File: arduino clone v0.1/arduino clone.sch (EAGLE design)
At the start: 21 parts, among them J202 FTDI Breakout Header, U101 ATMEGA328P_TQFP, U201 CH340G

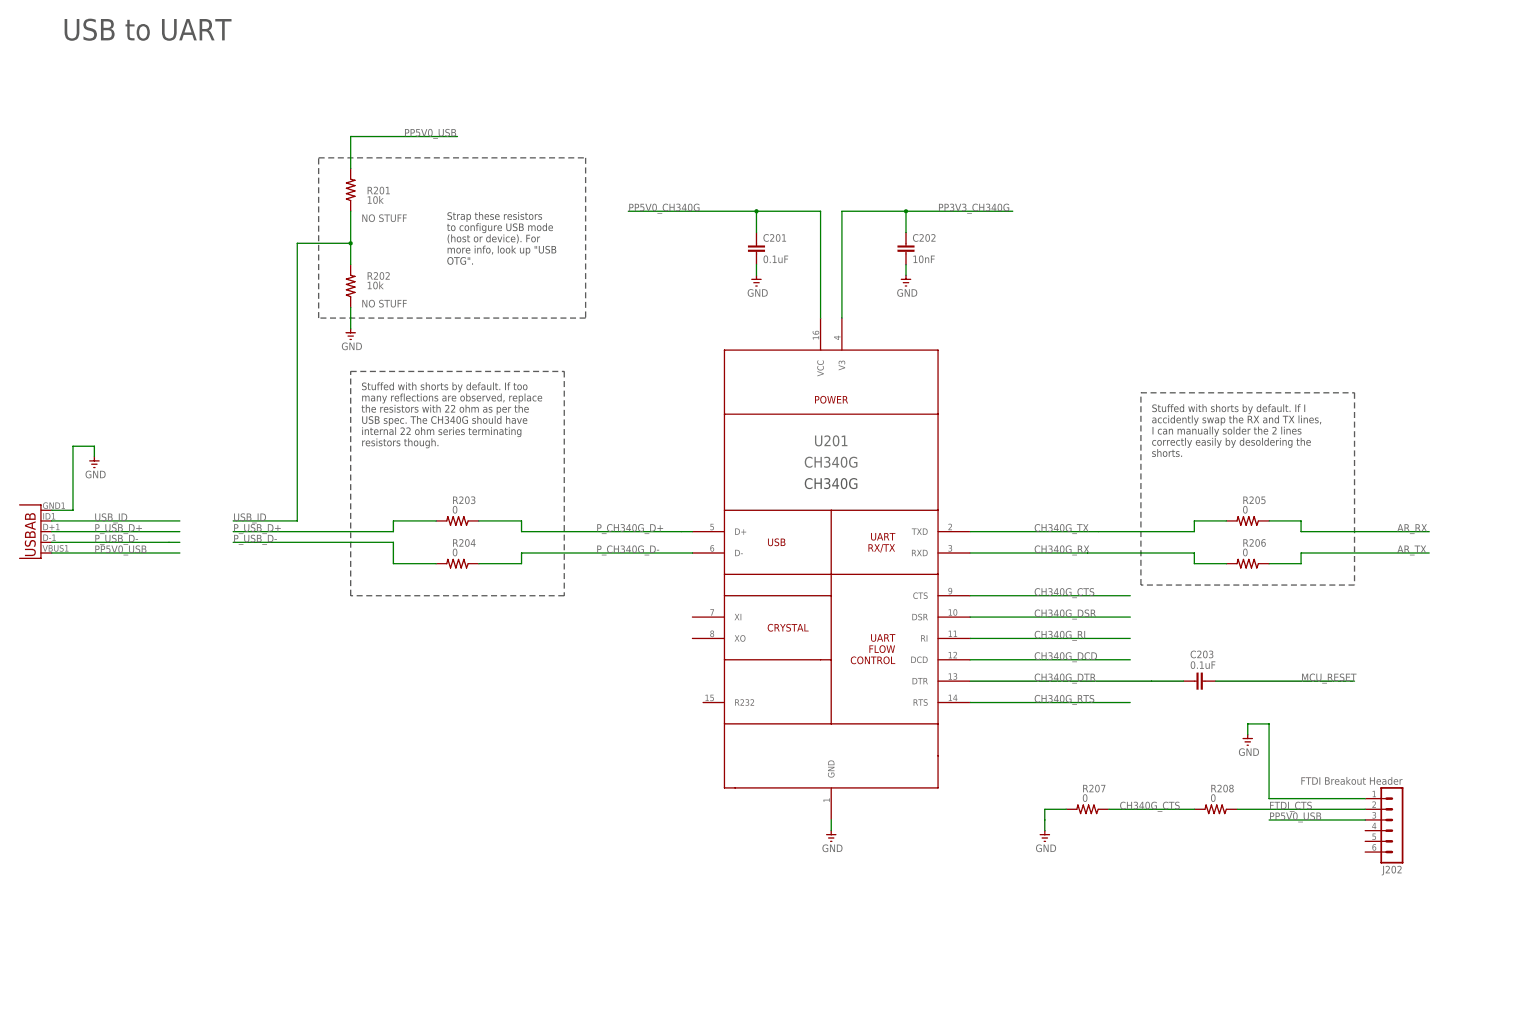
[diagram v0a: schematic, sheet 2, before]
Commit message: add FTDI RX and TX lines
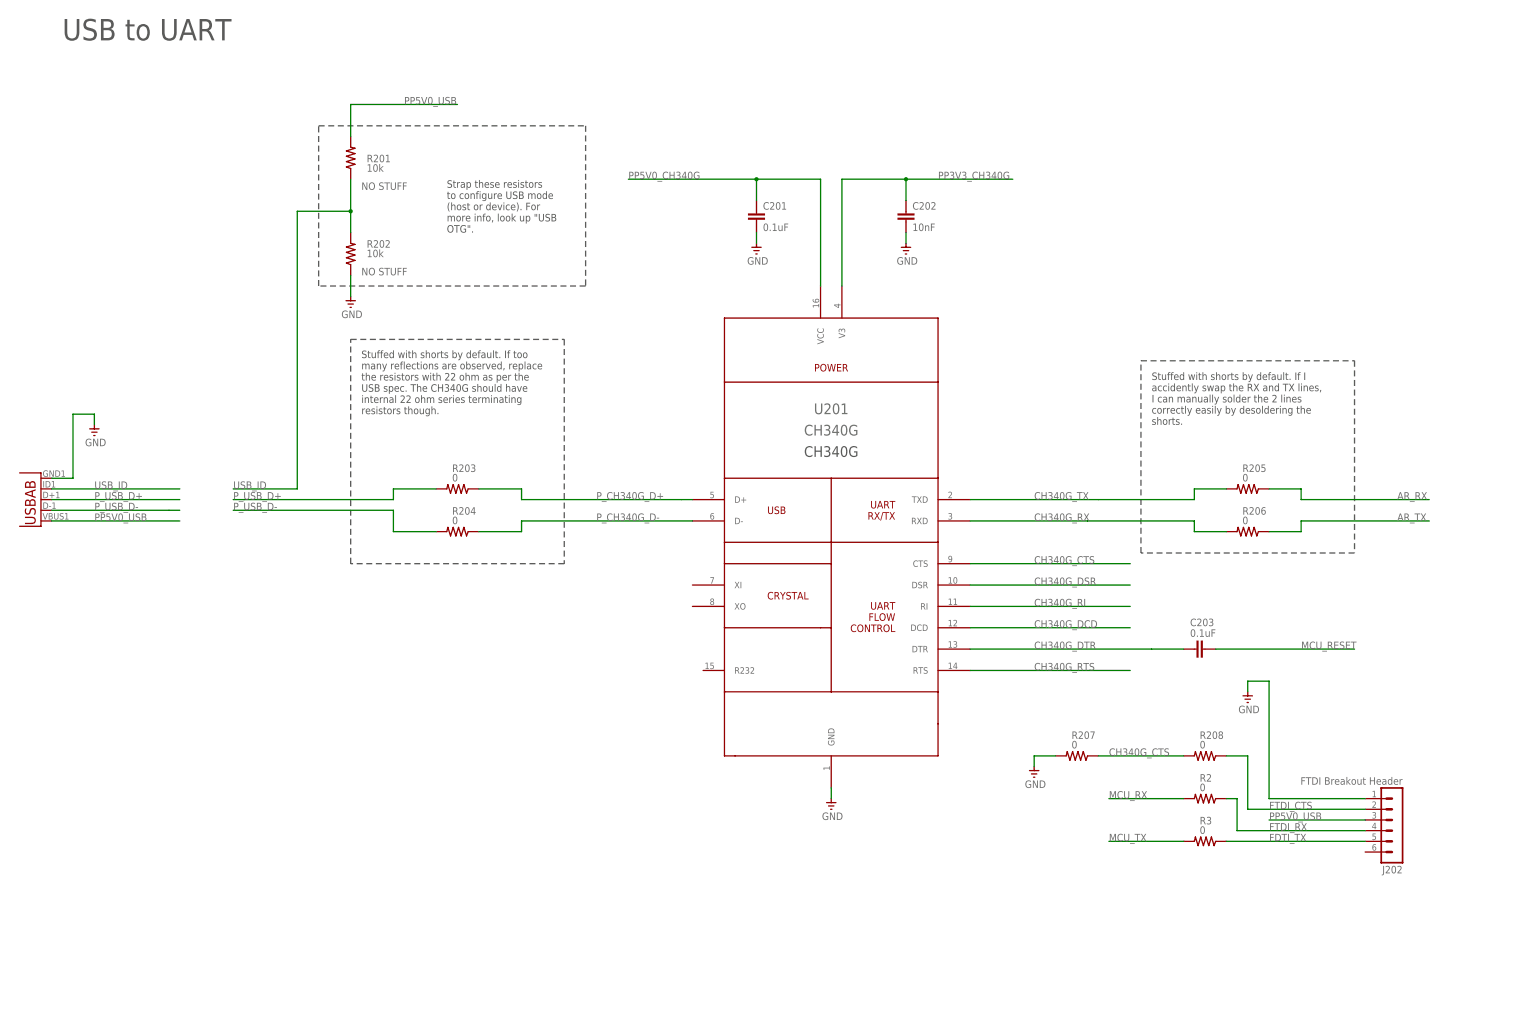
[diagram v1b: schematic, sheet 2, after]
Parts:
- added R2, R3: 0, adafruit:R-US_R0805
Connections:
- new net FDTI_TX: J202.5, R3.1
- new net FTDI_RX: J202.4, R2.1
- new net MCU_RX: R2.2
- new net MCU_TX: R3.2
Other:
- moved on the sheet: C201, C202, C203, R201, R202, R203, R204, R205, R206, R207, R208, U201

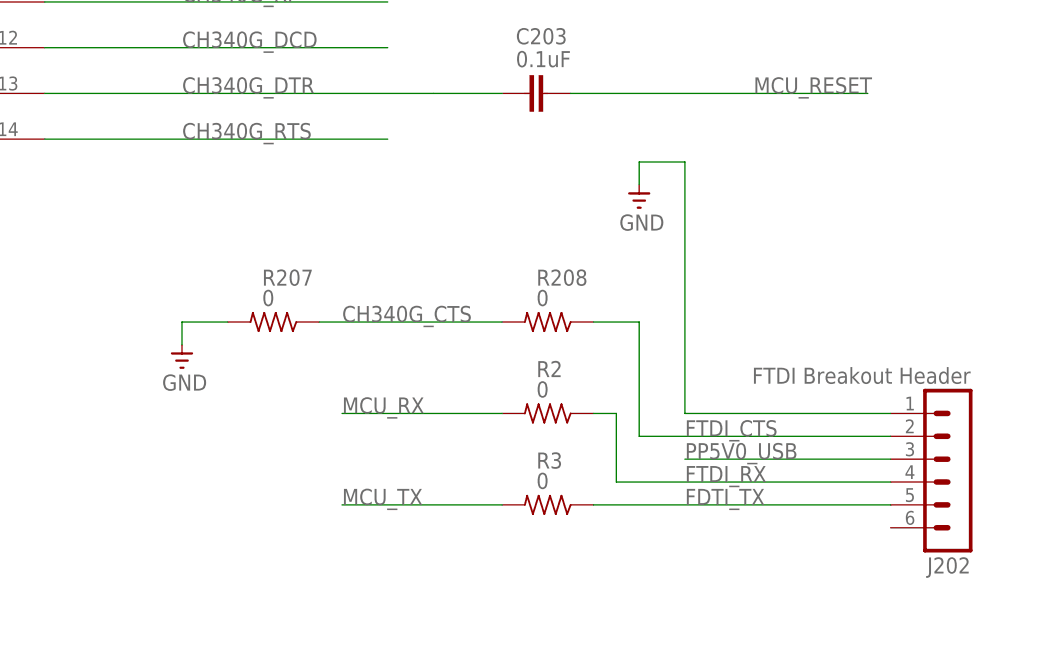
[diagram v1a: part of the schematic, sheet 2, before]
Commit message: add FTDI_DTR line
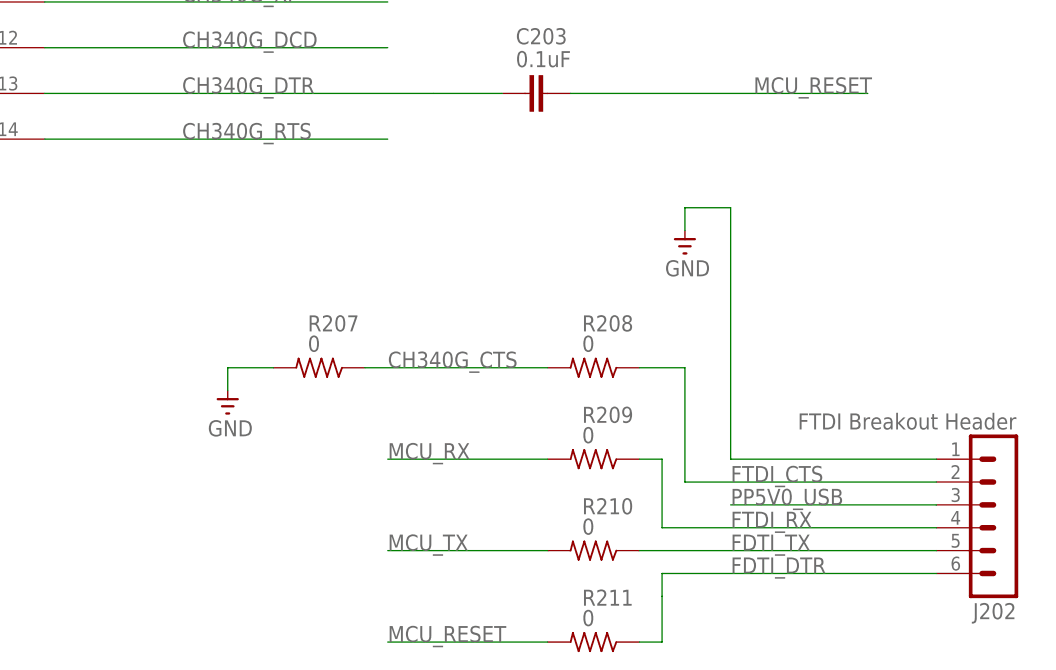
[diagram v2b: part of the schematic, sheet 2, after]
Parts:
- removed R2, R3: 0, adafruit:R-US_R0805
- added R209, R210, R211: 0, adafruit:R-US_R0805
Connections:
- new net FDTI_DTR: J202.6, R211.1
- net FDTI_TX: now also R210.1; no longer R3.1
- net FTDI_RX: now also R209.1; no longer R2.1
- net MCU_RESET: now also R211.2
- net MCU_RX: now also R209.2; no longer R2.2
- net MCU_TX: now also R210.2; no longer R3.2
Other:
- moved on the sheet: J202, R207, R208
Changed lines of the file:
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@@
 <part name="R207" library="adafruit" deviceset="R-US_" device="R0805" value="0"/>
 <part name="GND13" library="supply" deviceset="GND" device=""/>
-<part name="R2" library="adafruit" deviceset="R-US_" device="R0805" value="0"/>
-<part name="R3" library="adafruit" deviceset="R-US_" device="R0805" value="0"/>
+<part name="R209" library="adafruit" deviceset="R-US_" device="R0805" value="0"/>
+<part name="R210" library="adafruit" deviceset="R-US_" device="R0805" value="0"/>
+<part name="R211" library="adafruit" deviceset="R-US_" device="R0805" value="0"/>
 </parts>
 <sheets>
@@
 <attribute name="VALUE" x="293.624" y="96.901" size="1.778" layer="96"/>
 </instance>
-<instance part="J202" gate="1" x="342.9" y="50.8" rot="R180"/>
-<instance part="GND12" gate="1" x="307.34" y="81.28" smashed="yes">
-<attribute name="VALUE" x="305.1175" y="78.74" size="1.778" layer="96"/>
-</instance>
-<instance part="R208" gate="G$1" x="297.18" y="68.58" smashed="yes" rot="R180">
-<attribute name="NAME" x="295.91" y="72.6186" size="1.778" layer="95"/>
-<attribute name="VALUE" x="295.91" y="70.358" size="1.778" layer="96"/>
-</instance>
-<instance part="R207" gate="G$1" x="266.7" y="68.58" smashed="yes" rot="R180">
-<attribute name="NAME" x="265.43" y="72.6186" size="1.778" layer="95"/>
-<attribute name="VALUE" x="265.43" y="70.358" size="1.778" layer="96"/>
-</instance>
-<instance part="GND13" gate="1" x="256.54" y="63.5" smashed="yes">
-<attribute name="VALUE" x="254.3175" y="60.96" size="1.778" layer="96"/>
-</instance>
-<instance part="R2" gate="G$1" x="297.18" y="58.42" smashed="yes" rot="R180">
-<attribute name="NAME" x="295.91" y="62.4586" size="1.778" layer="95"/>
-<attribute name="VALUE" x="295.91" y="60.198" size="1.778" layer="96"/>
-</instance>
-<instance part="R3" gate="G$1" x="297.18" y="48.26" smashed="yes" rot="R180">
-<attribute name="NAME" x="295.91" y="52.2986" size="1.778" layer="95"/>
-<attribute name="VALUE" x="295.91" y="50.038" size="1.778" layer="96"/>
+<instance part="J202" gate="1" x="347.98" y="45.72" rot="R180"/>
+<instance part="GND12" gate="1" x="312.42" y="76.2" smashed="yes">
+<attribute name="VALUE" x="310.1975" y="73.66" size="1.778" layer="96"/>
+</instance>
+<instance part="R208" gate="G$1" x="302.26" y="63.5" smashed="yes" rot="R180">
+<attribute name="NAME" x="300.99" y="67.5386" size="1.778" layer="95"/>
+<attribute name="VALUE" x="300.99" y="65.278" size="1.778" layer="96"/>
+</instance>
+<instance part="R207" gate="G$1" x="271.78" y="63.5" smashed="yes" rot="R180">
+<attribute name="NAME" x="270.51" y="67.5386" size="1.778" layer="95"/>
+<attribute name="VALUE" x="270.51" y="65.278" size="1.778" layer="96"/>
+</instance>
+<instance part="GND13" gate="1" x="261.62" y="58.42" smashed="yes">
+<attribute name="VALUE" x="259.3975" y="55.88" size="1.778" layer="96"/>
+</instance>
+<instance part="R209" gate="G$1" x="302.26" y="53.34" smashed="yes" rot="R180">
+<attribute name="NAME" x="300.99" y="57.3786" size="1.778" layer="95"/>
+<attribute name="VALUE" x="300.99" y="55.118" size="1.778" layer="96"/>
+</instance>
+<instance part="R210" gate="G$1" x="302.26" y="43.18" smashed="yes" rot="R180">
+<attribute name="NAME" x="300.99" y="47.2186" size="1.778" layer="95"/>
+<attribute name="VALUE" x="300.99" y="44.958" size="1.778" layer="96"/>
+</instance>
+<instance part="R211" gate="G$1" x="302.26" y="33.02" smashed="yes" rot="R180">
+<attribute name="NAME" x="300.99" y="37.0586" size="1.778" layer="95"/>
+<attribute name="VALUE" x="300.99" y="34.798" size="1.778" layer="96"/>
 </instance>
 </instances>
@@
 </segment>
 <segment>
-<wire x1="307.34" y1="86.36" x2="312.42" y2="86.36" width="0.1524" layer="91"/>
-<wire x1="312.42" y1="86.36" x2="312.42" y2="58.42" width="0.1524" layer="91"/>
+<wire x1="312.42" y1="81.28" x2="317.5" y2="81.28" width="0.1524" layer="91"/>
+<wire x1="317.5" y1="81.28" x2="317.5" y2="53.34" width="0.1524" layer="91"/>
 <pinref part="J202" gate="1" pin="1"/>
-<wire x1="312.42" y1="58.42" x2="335.28" y2="58.42" width="0.1524" layer="91"/>
+<wire x1="317.5" y1="53.34" x2="340.36" y2="53.34" width="0.1524" layer="91"/>
 <pinref part="GND12" gate="1" pin="GND"/>
-<wire x1="307.34" y1="83.82" x2="307.34" y2="86.36" width="0.1524" layer="91"/>
+<wire x1="312.42" y1="78.74" x2="312.42" y2="81.28" width="0.1524" layer="91"/>
 </segment>
 <segment>
 <pinref part="R207" gate="G$1" pin="2"/>
-<wire x1="256.54" y1="68.58" x2="261.62" y2="68.58" width="0.1524" layer="91"/>
+<wire x1="261.62" y1="63.5" x2="266.7" y2="63.5" width="0.1524" layer="91"/>
 <pinref part="GND13" gate="1" pin="GND"/>
-<wire x1="256.54" y1="66.04" x2="256.54" y2="68.58" width="0.1524" layer="91"/>
+<wire x1="261.62" y1="60.96" x2="261.62" y2="63.5" width="0.1524" layer="91"/>
 </segment>
 </net>
@@
 <segment>
 <pinref part="J202" gate="1" pin="3"/>
-<wire x1="335.28" y1="53.34" x2="312.42" y2="53.34" width="0.1524" layer="91"/>
-<label x="312.42" y="53.34" size="1.778" layer="95"/>
+<wire x1="340.36" y1="48.26" x2="317.5" y2="48.26" width="0.1524" layer="91"/>
+<label x="317.5" y="48.26" size="1.778" layer="95"/>
 </segment>
 </net>
@@
 <label x="320.04" y="93.98" size="1.778" layer="95"/>
 </segment>
+<segment>
+<pinref part="R211" gate="G$1" pin="2"/>
+<wire x1="297.18" y1="33.02" x2="279.4" y2="33.02" width="0.1524" layer="91"/>
+<label x="279.4" y="33.02" size="1.778" layer="95"/>
+</segment>
 </net>
 <net name="CH340G_CTS" class="0">
@@
 <pinref part="R207" gate="G$1" pin="1"/>
 <pinref part="R208" gate="G$1" pin="2"/>
-<wire x1="271.78" y1="68.58" x2="292.1" y2="68.58" width="0.1524" layer="91"/>
-<label x="274.32" y="68.58" size="1.778" layer="95"/>
+<wire x1="276.86" y1="63.5" x2="297.18" y2="63.5" width="0.1524" layer="91"/>
+<label x="279.4" y="63.5" size="1.778" layer="95"/>
 </segment>
 </net>
@@
 <segment>
 <pinref part="J202" gate="1" pin="4"/>
-<wire x1="335.28" y1="50.8" x2="304.8" y2="50.8" width="0.1524" layer="91"/>
-<label x="312.42" y="50.8" size="1.778" layer="95"/>
-<pinref part="R2" gate="G$1" pin="1"/>
-<wire x1="302.26" y1="58.42" x2="304.8" y2="58.42" width="0.1524" layer="91"/>
-<wire x1="304.8" y1="58.42" x2="304.8" y2="50.8" width="0.1524" layer="91"/>
+<wire x1="340.36" y1="45.72" x2="309.88" y2="45.72" width="0.1524" layer="91"/>
+<label x="317.5" y="45.72" size="1.778" layer="95"/>
+<pinref part="R209" gate="G$1" pin="1"/>
+<wire x1="307.34" y1="53.34" x2="309.88" y2="53.34" width="0.1524" layer="91"/>
+<wire x1="309.88" y1="53.34" x2="309.88" y2="45.72" width="0.1524" layer="91"/>
 </segment>
 </net>
@@
 <segment>
 <pinref part="R208" gate="G$1" pin="1"/>
-<wire x1="302.26" y1="68.58" x2="307.34" y2="68.58" width="0.1524" layer="91"/>
-<wire x1="307.34" y1="68.58" x2="307.34" y2="55.88" width="0.1524" layer="91"/>
+<wire x1="307.34" y1="63.5" x2="312.42" y2="63.5" width="0.1524" layer="91"/>
+<wire x1="312.42" y1="63.5" x2="312.42" y2="50.8" width="0.1524" layer="91"/>
 <pinref part="J202" gate="1" pin="2"/>
-<wire x1="307.34" y1="55.88" x2="335.28" y2="55.88" width="0.1524" layer="91"/>
-<label x="312.42" y="55.88" size="1.778" layer="95"/>
+<wire x1="312.42" y1="50.8" x2="340.36" y2="50.8" width="0.1524" layer="91"/>
+<label x="317.5" y="50.8" size="1.778" layer="95"/>
 </segment>
 </net>
 <net name="MCU_RX" class="0">
 <segment>
-<pinref part="R2" gate="G$1" pin="2"/>
-<wire x1="292.1" y1="58.42" x2="274.32" y2="58.42" width="0.1524" layer="91"/>
-<label x="274.32" y="58.42" size="1.778" layer="95"/>
+<pinref part="R209" gate="G$1" pin="2"/>
+<wire x1="297.18" y1="53.34" x2="279.4" y2="53.34" width="0.1524" layer="91"/>
+<label x="279.4" y="53.34" size="1.778" layer="95"/>
 </segment>
 </net>
 <net name="FDTI_TX" class="0">
 <segment>
-<pinref part="R3" gate="G$1" pin="1"/>
+<pinref part="R210" gate="G$1" pin="1"/>
 <pinref part="J202" gate="1" pin="5"/>
-<wire x1="302.26" y1="48.26" x2="335.28" y2="48.26" width="0.1524" layer="91"/>
-<label x="312.42" y="48.26" size="1.778" layer="95"/>
+<wire x1="307.34" y1="43.18" x2="340.36" y2="43.18" width="0.1524" layer="91"/>
+<label x="317.5" y="43.18" size="1.778" layer="95"/>
 </segment>
 </net>
 <net name="MCU_TX" class="0">
 <segment>
-<pinref part="R3" gate="G$1" pin="2"/>
-<wire x1="292.1" y1="48.26" x2="274.32" y2="48.26" width="0.1524" layer="91"/>
-<label x="274.32" y="48.26" size="1.778" layer="95"/>
-</segment>
-</net>
+<pinref part="R210" gate="G$1" pin="2"/>
+<wire x1="297.18" y1="43.18" x2="279.4" y2="43.18" width="0.1524" layer="91"/>
+<label x="279.4" y="43.18" size="1.778" layer="95"/>
+</segment>
+</net>
+<net name="FDTI_DTR" class="0">
+<segment>
+<pinref part="R211" gate="G$1" pin="1"/>
+<wire x1="307.34" y1="33.02" x2="309.88" y2="33.02" width="0.1524" layer="91"/>
+<wire x1="309.88" y1="33.02" x2="309.88" y2="38.1" width="0.1524" layer="91"/>
+<wire x1="309.88" y1="38.1" x2="309.88" y2="40.64" width="0.1524" layer="91"/>
+<pinref part="J202" gate="1" pin="6"/>
+<wire x1="309.88" y1="40.64" x2="340.36" y2="40.64" width="0.1524" layer="91"/>
+<label x="317.5" y="40.64" size="1.778" layer="95"/>
+</segment>
+</net>
